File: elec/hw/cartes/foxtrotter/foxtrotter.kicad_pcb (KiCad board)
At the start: 2 copper layers, 40 x 35 mm, 17 parts, among them J1 22053061, U2 SCH16T-K01-10

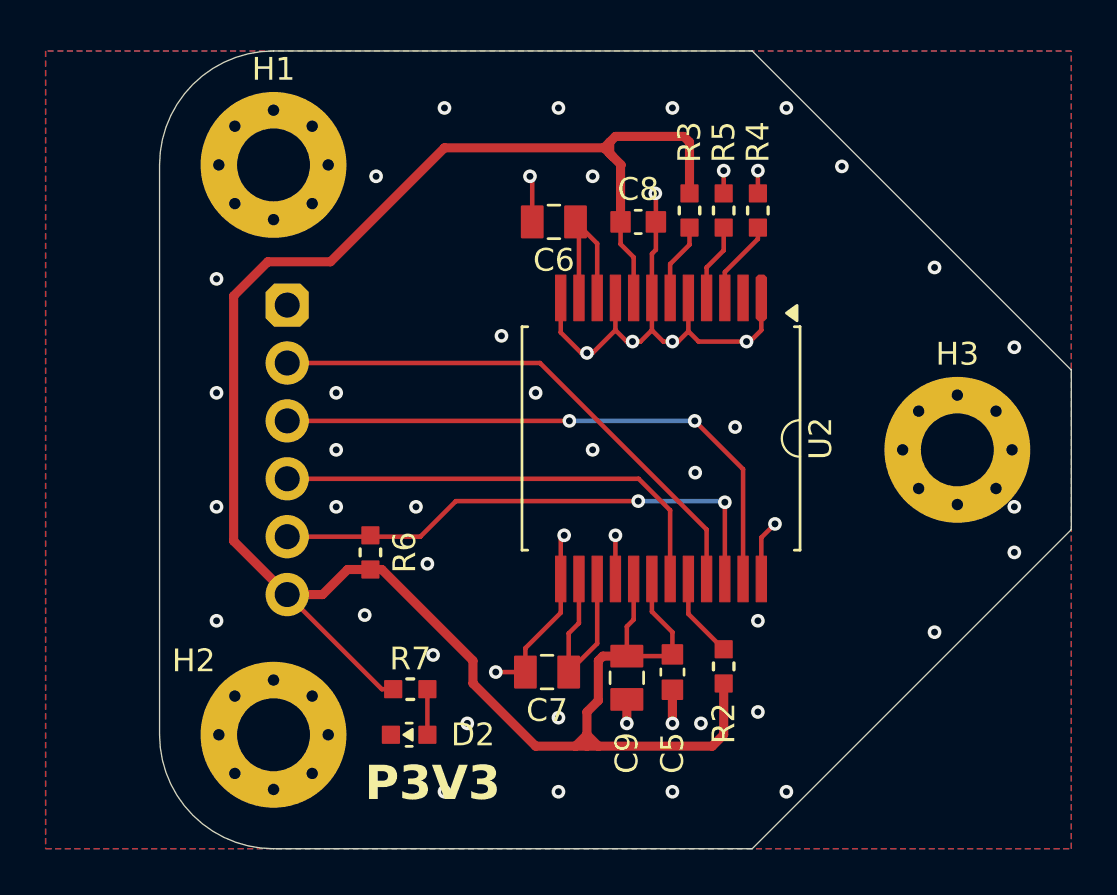
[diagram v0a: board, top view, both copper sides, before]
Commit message: foxtrotter : mounting holes changed to M2
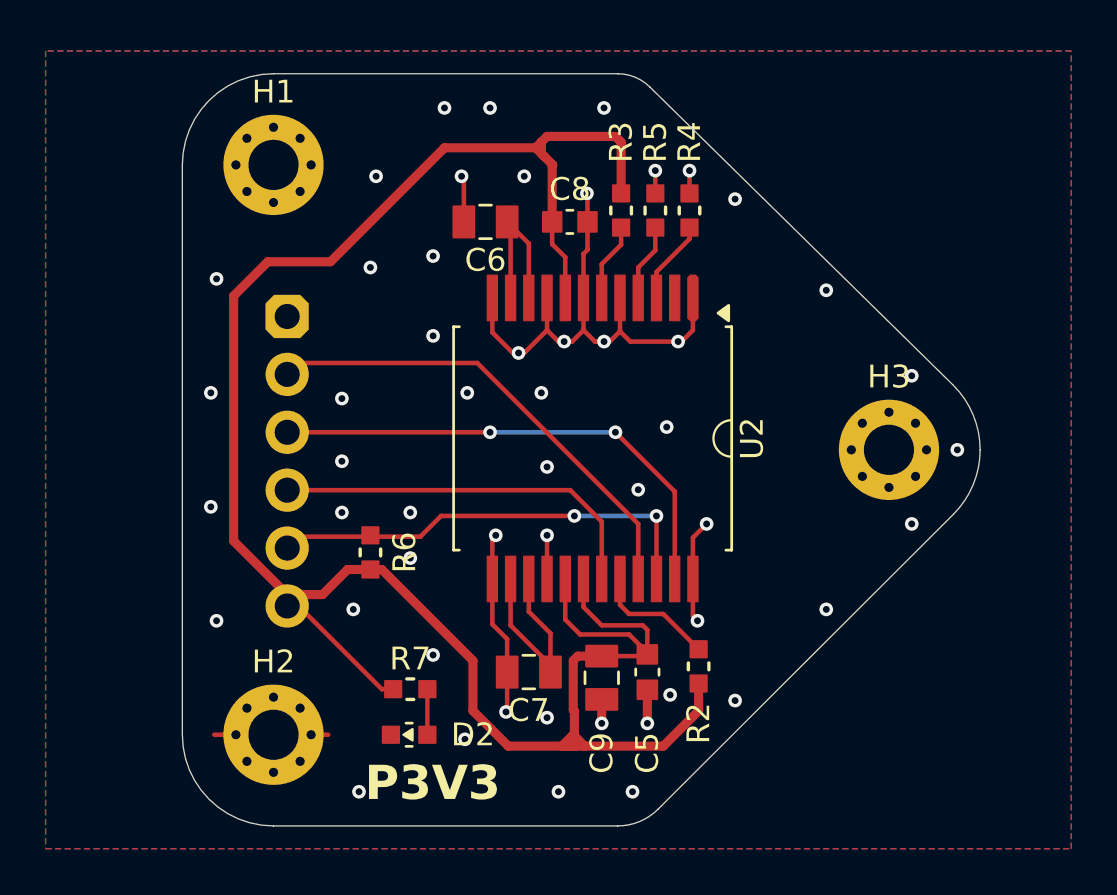
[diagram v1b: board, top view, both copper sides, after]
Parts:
- H1, H2, H3: value MountingHole_Pad_M3 -> MountingHole_Pad_M2; footprint cocotter_others:MountingHole_3.2mm_M3_Pad_Via -> cocotter_others:MountingHole_2.2mm_M2_Pad_Via
- moved C6 3.00 mm to (99.3, 47.5)
- moved C8 3.00 mm to (103.0, 47.5)
- moved H3 3.00 mm to (117.0, 57.5)
- moved R3 3.00 mm to (105.2, 47.0)
- moved R4 3.00 mm to (108.2, 47.0)
- moved R5 3.00 mm to (106.8, 47.0)
- moved U2 3.00 mm to (104.0, 57.0)
- moved C5 1.10 mm to (106.4, 67.2)
- moved C9 1.10 mm to (104.4, 67.5)
- moved R2 1.10 mm to (108.7, 67.0)
- moved C7 0.80 mm to (101.2, 67.2)
- moved J1 0.50 mm to (90.6, 58.0)
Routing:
- net //gyro_cs_3v3: track 23.3 -> 19.3 mm
- net /gyro_mosi_3v3: track 25.7 -> 21.9 mm
- net /gyro_miso_3v3: track 20.4 -> 16.9 mm
- net /gyro_sck_3v3: track 23.6 -> 20.7 mm
- net GND: track 46.8 -> 48.8 mm, vias 51 -> 52
- net Net-(U2-DRY/SYNC): track 3.73 -> 5.39 mm
- net +3V3: track 95.3 -> 96.1 mm
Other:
- board size 40 x 35 mm -> 35 x 33 mm

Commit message: foxtrotter board updated with jlcpcb parts
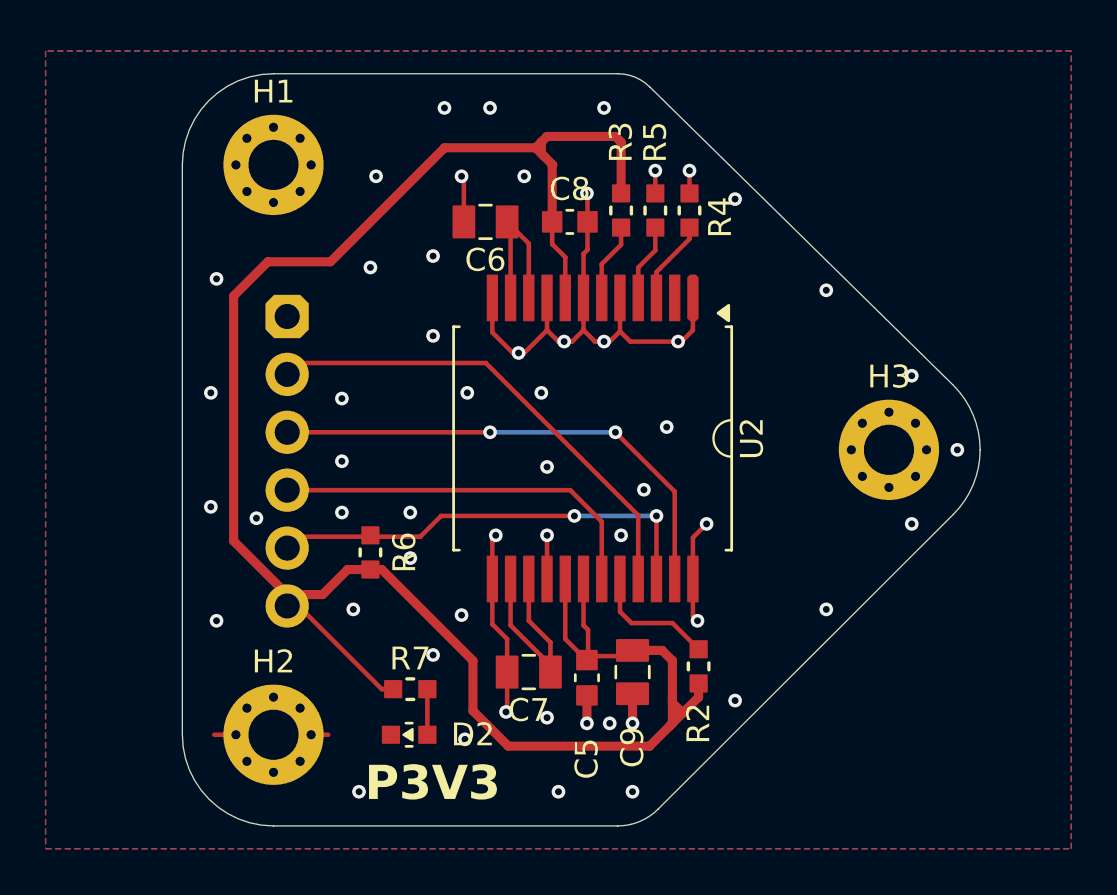
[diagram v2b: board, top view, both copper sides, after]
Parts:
- moved C5 2.66 mm to (103.8, 67.5)
- moved C9 1.37 mm to (105.8, 67.2)
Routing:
- net +3V3: track 96.1 -> 90.4 mm
- net GND: vias 52 -> 55

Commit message: board name added
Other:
- board text added: "FOXTR'OTTER 2026"
- board text added: "SCH16T-K01-10"
